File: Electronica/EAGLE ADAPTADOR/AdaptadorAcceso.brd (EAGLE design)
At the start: 60 x 49 mm, 9 parts

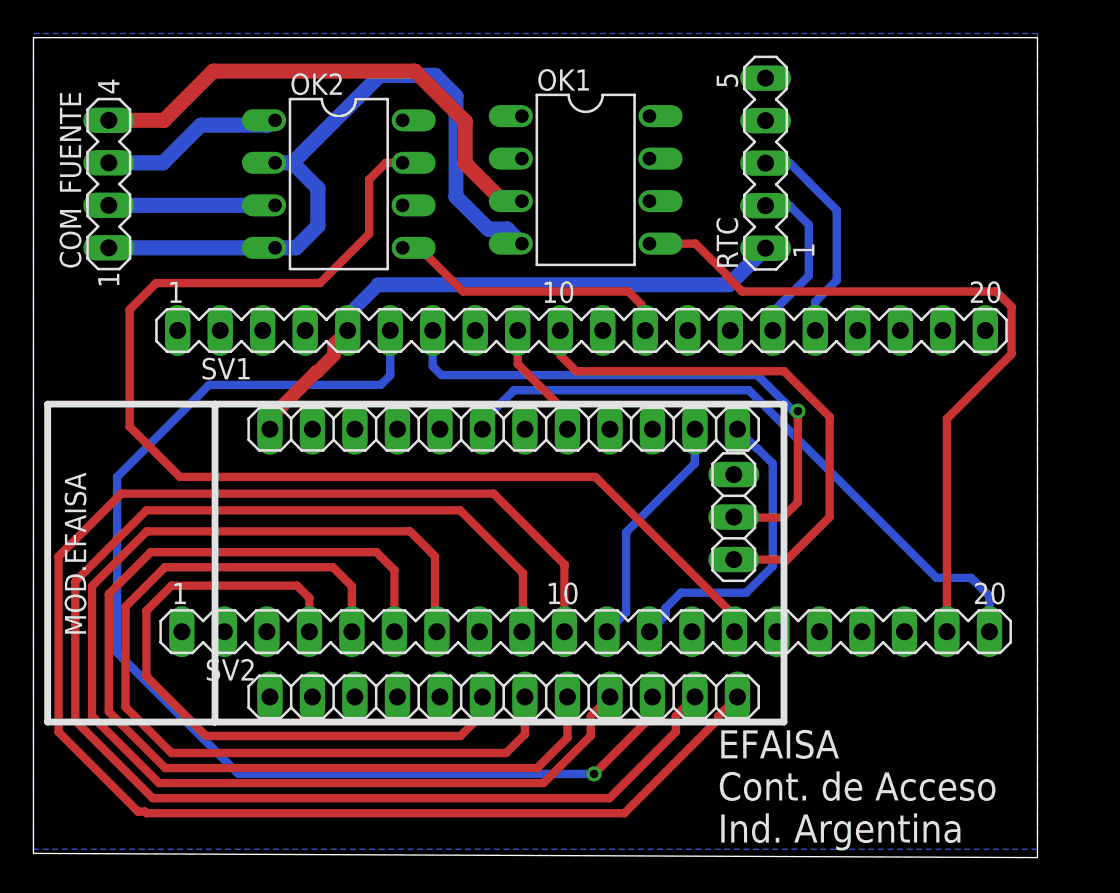
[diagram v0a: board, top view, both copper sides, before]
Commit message: PCB terminado, archivos Gerber generados
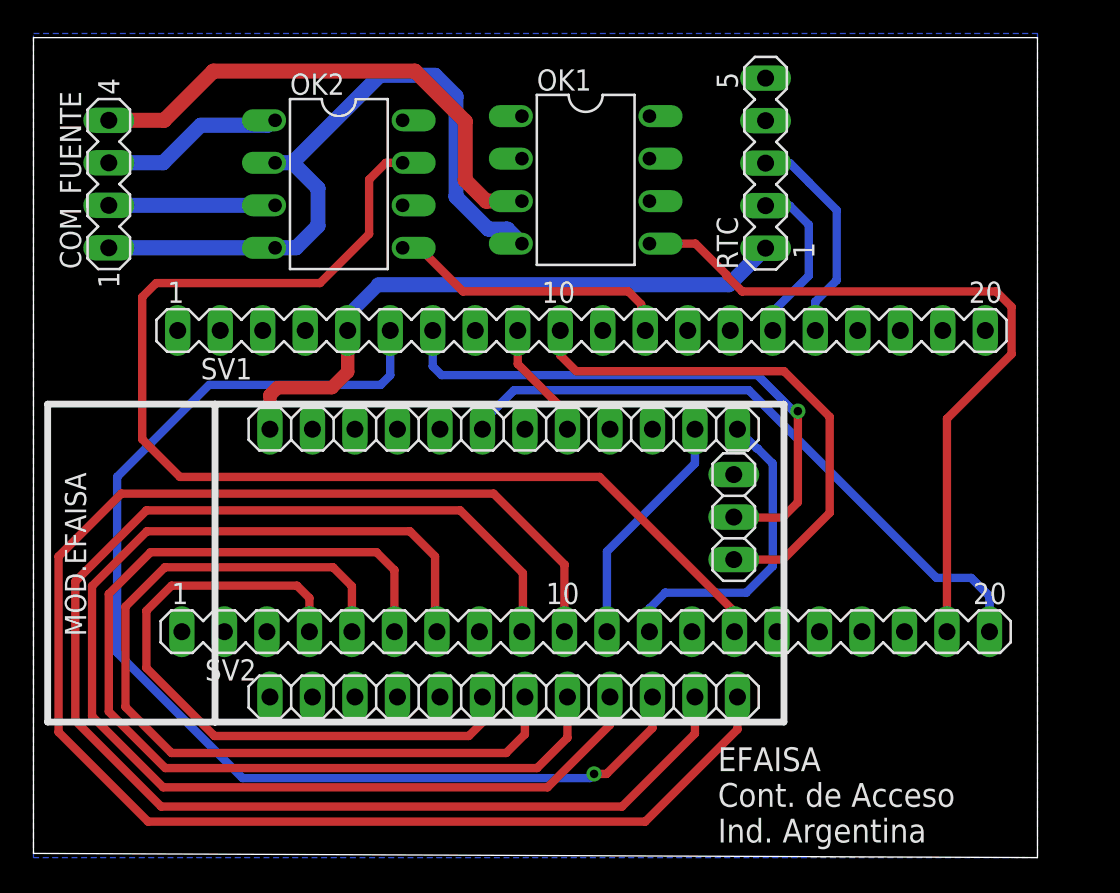
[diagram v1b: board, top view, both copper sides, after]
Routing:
- net +3V3: track 35.4 -> 37.3 mm
- net IO41: track 93.6 -> 95.1 mm
- net IO42: track 83.9 -> 85.1 mm
- net IO21: track 69.6 -> 70.2 mm
- net N$1: track 30.6 -> 31.2 mm
- net IO39: track 18.3 -> 18.9 mm
